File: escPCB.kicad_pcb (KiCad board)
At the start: 2 copper layers, 69 parts, among them IC1 W25Q16JVSNIQ, J1 Terminal, J2 2137160001, J3 XT60-M, J4 Conn_01x03_Pin, J5 Conn_01x03_Pin, J6 Conn_01x02_Pin, Q1 BC857, Q10 BC857, Q11 BC857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

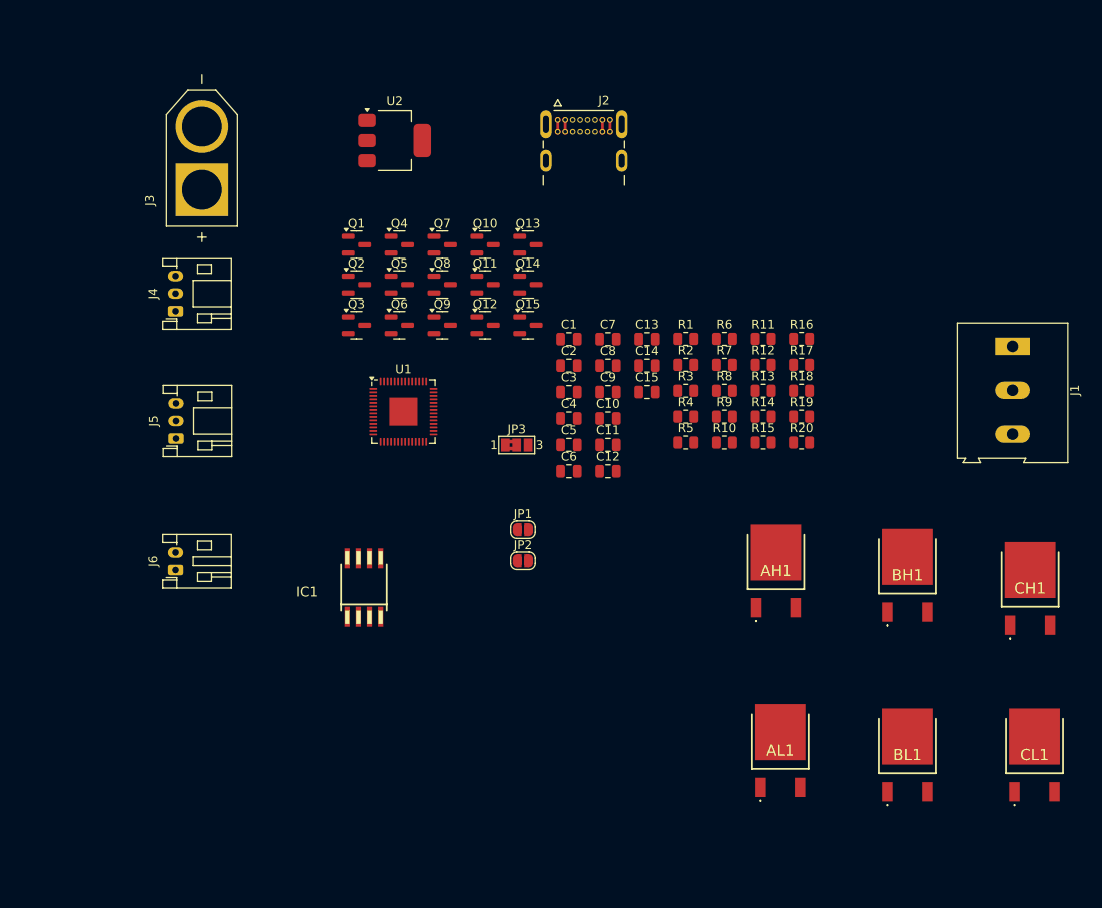
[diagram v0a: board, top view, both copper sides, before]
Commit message: v3 PCB design from Desktop
Had to upload differently cause it was made on my desktop
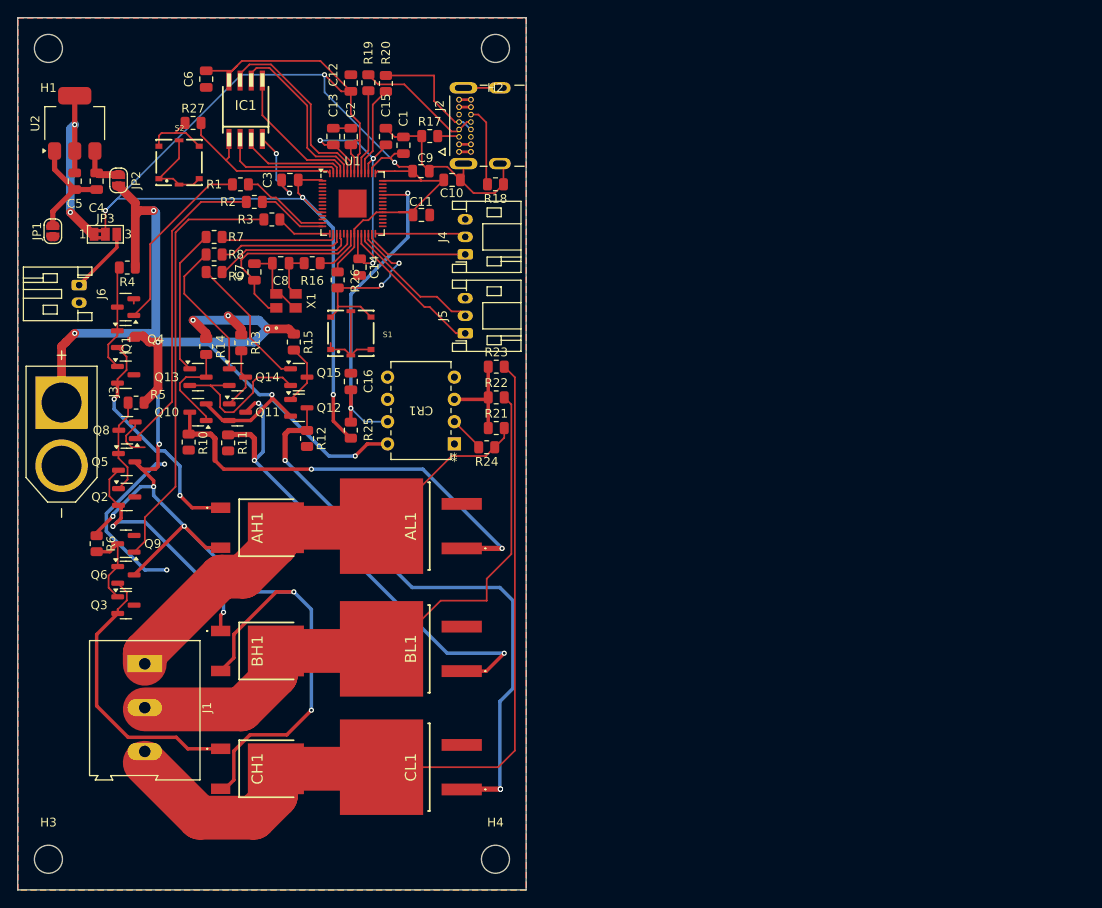
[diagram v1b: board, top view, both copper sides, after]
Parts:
- added C16: C, Capacitor_SMD:C_0805_2012Metric, F.Cu at (98.0, 90.5)
- added CR1: LM211N, SPROGEE3:DIP-8_STM, F.Cu at (109.8, 97.6)
- added H1: MountingHole, MountingHole:MountingHole_3.2mm_M3, F.Cu at (63.5, 52.5)
- added H2: MountingHole, MountingHole:MountingHole_3.2mm_M3, F.Cu at (114.5, 52.5)
- added H3: MountingHole, MountingHole:MountingHole_3.2mm_M3, F.Cu at (63.5, 145.0)
- added H4: MountingHole, MountingHole:MountingHole_3.2mm_M3, F.Cu at (114.5, 145.0)
- added R21: 33k, Resistor_SMD:R_0805_2012Metric, F.Cu at (114.6, 95.8)
- added R22: 33k, Resistor_SMD:R_0805_2012Metric, F.Cu at (114.6, 92.3)
- added R23: 33k, Resistor_SMD:R_0805_2012Metric, F.Cu at (114.6, 88.8)
- added R24: 33k, Resistor_SMD:R_0805_2012Metric, F.Cu at (113.5, 98.0)
- added R25: 1k, Resistor_SMD:R_0805_2012Metric, F.Cu at (98.0, 96.0)
- added R26: 10k, Resistor_SMD:R_0805_2012Metric, F.Cu at (96.5, 78.9)
- added R27: 1k, Resistor_SMD:R_0805_2012Metric, F.Cu at (80.0, 61.0)
- added S1: 431183015816, SPROGEE3:431183015816, F.Cu at (98.0, 85.0)
- added S2: 431183015816, SPROGEE3:431183015816, F.Cu at (78.4, 65.5)
- AL1, BL1, CL1: footprint SPROGEE3:IPD70P04P4L08ATMA2 -> SPROGEE3:IPB70N12S311ATMA1
- X1: footprint Library:ABM8-272-T3_ABR -> SPROGEE3:ABM8-272-T3_ABR
- moved J1 105.4 mm to (74.5, 122.7)
- moved CH1 89.8 mm to (88.4, 134.7), turned to -90 degrees
- moved R6 75.3 mm to (69.0, 109.0), turned to -90 degrees
- moved BH1 73.8 mm to (88.4, 121.2), turned to -90 degrees
- moved CL1 71.8 mm to (104.2, 134.5), turned to 90 degrees
- moved R4 65.9 mm to (72.5, 77.5), turned to 180 degrees
- moved R14 64.0 mm to (81.5, 86.5), turned to -90 degrees
- moved C5 63.9 mm to (66.5, 67.7), turned to -90 degrees
- moved JP1 63.5 mm to (64.0, 73.3), turned to 90 degrees
- moved JP2 63.3 mm to (71.5, 67.5), turned to -90 degrees
- moved R5 62.9 mm to (73.5, 92.9), turned to 180 degrees
- moved R20 62.7 mm to (102.0, 56.5), turned to -90 degrees
- moved R19 62.4 mm to (100.0, 56.4), turned to -90 degrees
- moved R11 62.2 mm to (84.0, 97.5), turned to -90 degrees
- moved R10 61.1 mm to (79.5, 97.4), turned to -90 degrees
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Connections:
- net Net-(AH1-S) renamed L1
- net Net-(BH1-S) renamed L2
- net Net-(CH1-S) renamed L3
- JP3 pad 2: Net-(J6-Pin_1) -> +3.3V
- JP3 pad 3: +3.3V -> Net-(J6-Pin_1)
- U1 pad 26: unconnected-(U1-RUN-Pad26) -> Net-(U1-RUN)
- U1 pad 38: unconnected-(U1-GPIO26_ADC0-Pad38) -> PHASED
- U1 pad 44: unconnected-(U1-VREG_IN-Pad44) -> +3.3V
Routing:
- net +BATT: track 0.00 -> 245.8 mm, vias 0 -> 14
- net +3.3V: track 0.00 -> 188.0 mm, vias 0 -> 5
- net L3: track 0.00 -> 98.3 mm
- net GND: track 0.00 -> 94.6 mm, vias 0 -> 4
- net L2: track 0.00 -> 73.7 mm
- net CL_Gate: track 0.00 -> 67.5 mm, vias 0 -> 3
- net BL_Gate: track 0.00 -> 58.1 mm, vias 0 -> 3
- net L1: track 0.00 -> 55.3 mm
- net AL_Gate: track 0.00 -> 50.0 mm, vias 0 -> 2
- net Net-(Q9-B): track 0.00 -> 49.1 mm
- net PHASED: track 0.00 -> 38.7 mm, vias 0 -> 2
- net Net-(Q8-B): track 0.00 -> 35.3 mm
- net +1V1: track 0.00 -> 33.9 mm, vias 0 -> 3
- net CH_Gate: track 0.00 -> 32.5 mm
- net BH_Gate: track 0.00 -> 27.9 mm, vias 0 -> 2
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- added copper zone on B.Cu, net GND
- added copper zone on F.Cu, net GND
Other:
- board outline added: 58 x 99.5 mm
